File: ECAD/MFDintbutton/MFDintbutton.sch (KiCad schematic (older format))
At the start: 35 parts, among them J1 Conn_02x03_Odd_Even, J2 Conn_01x04, J3 Conn_01x04, J4 Conn_01x04, SW11 SW_Push, SW12 SW_Push, SW13 SW_Push, SW14 SW_Push, SW21 SW_Push, SW22 SW_Push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

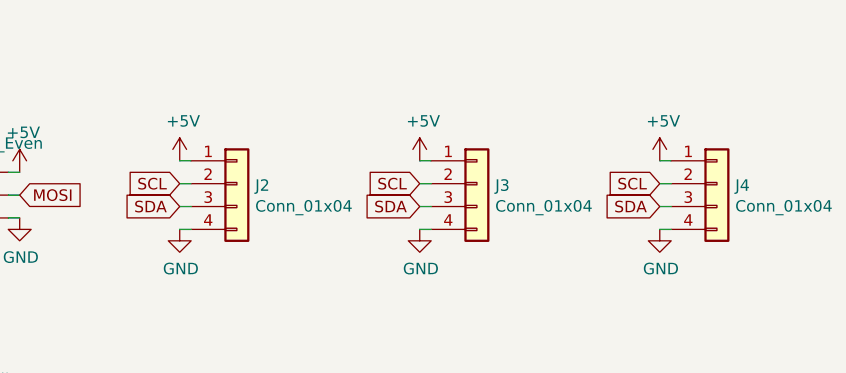
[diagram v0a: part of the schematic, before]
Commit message: Removing panelisations, adding polyfuses
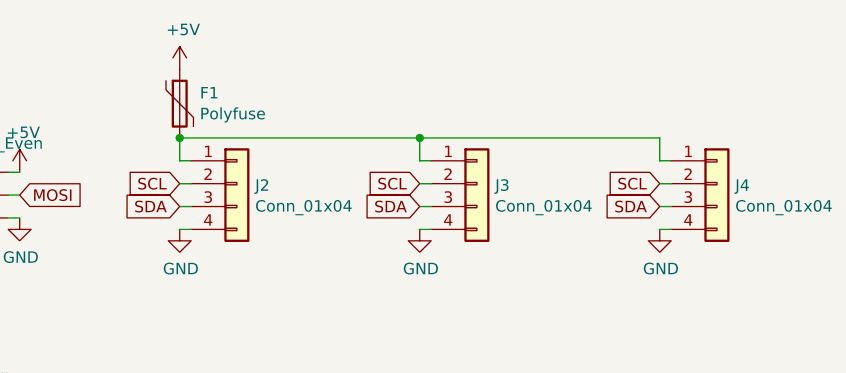
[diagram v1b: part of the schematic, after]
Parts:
- added F1: Polyfuse, Fuse:Fuse_1206_3216Metric_Pad1.42x1.75mm_HandSolder, symbol Device:Polyfuse
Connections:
- wire segments 141 -> 146
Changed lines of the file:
@@
 L power:+5V #PWR0104
 U 1 1 60C40200
-P 4650 1150
-F 0 "#PWR0104" H 4650 1000 50  0001 C CNN
-F 1 "+5V" H 4665 1323 50  0000 C CNN
-F 2 "" H 4650 1150 50  0001 C CNN
-F 3 "" H 4650 1150 50  0001 C CNN
-	1    4650 1150
+P 4650 750
+F 0 "#PWR0104" H 4650 600 50  0001 C CNN
+F 1 "+5V" H 4665 923 50  0000 C CNN
+F 2 "" H 4650 750 50  0001 C CNN
+F 3 "" H 4650 750 50  0001 C CNN
+	1    4650 750
 	1    0    0    -1
 $EndComp
@@
 	1    0    0    -1
 $EndComp
-$Comp
-L power:+5V #PWR0112
-U 1 1 60D32708
-P 5700 1150
-F 0 "#PWR0112" H 5700 1000 50  0001 C CNN
-F 1 "+5V" H 5715 1323 50  0000 C CNN
-F 2 "" H 5700 1150 50  0001 C CNN
-F 3 "" H 5700 1150 50  0001 C CNN
-	1    5700 1150
-	1    0    0    -1
-$EndComp
 Wire Wire Line
 	5700 1150 5750 1150
@@
 	1    0    0    -1
 $EndComp
-$Comp
-L power:+5V #PWR0114
-U 1 1 60D3B723
-P 6750 1150
-F 0 "#PWR0114" H 6750 1000 50  0001 C CNN
-F 1 "+5V" H 6765 1323 50  0000 C CNN
-F 2 "" H 6750 1150 50  0001 C CNN
-F 3 "" H 6750 1150 50  0001 C CNN
-	1    6750 1150
-	1    0    0    -1
-$EndComp
 Wire Wire Line
 	6750 1150 6800 1150
@@
 Wire Wire Line
 	6800 1450 6750 1450
+Wire Wire Line
+	6750 1150 6750 1050
+Wire Wire Line
+	6750 1050 5700 1050
+Wire Wire Line
+	5700 1050 5700 1150
+Wire Wire Line
+	4650 1150 4650 1050
+Wire Wire Line
+	4650 1050 5700 1050
+Connection ~ 5700 1050
+$Comp
+L Device:Polyfuse F1
+U 1 1 60FA5A26
+P 4650 900
+F 0 "F1" H 4738 946 50  0000 L CNN
+F 1 "Polyfuse" H 4738 855 50  0000 L CNN
+F 2 "Fuse:Fuse_1206_3216Metric_Pad1.42x1.75mm_HandSolder" H 4700 700 50  0001 L CNN
+F 3 "~" H 4650 900 50  0001 C CNN
+	1    4650 900
+	1    0    0    -1
+$EndComp
+Connection ~ 4650 1050
 $EndSCHEMATC

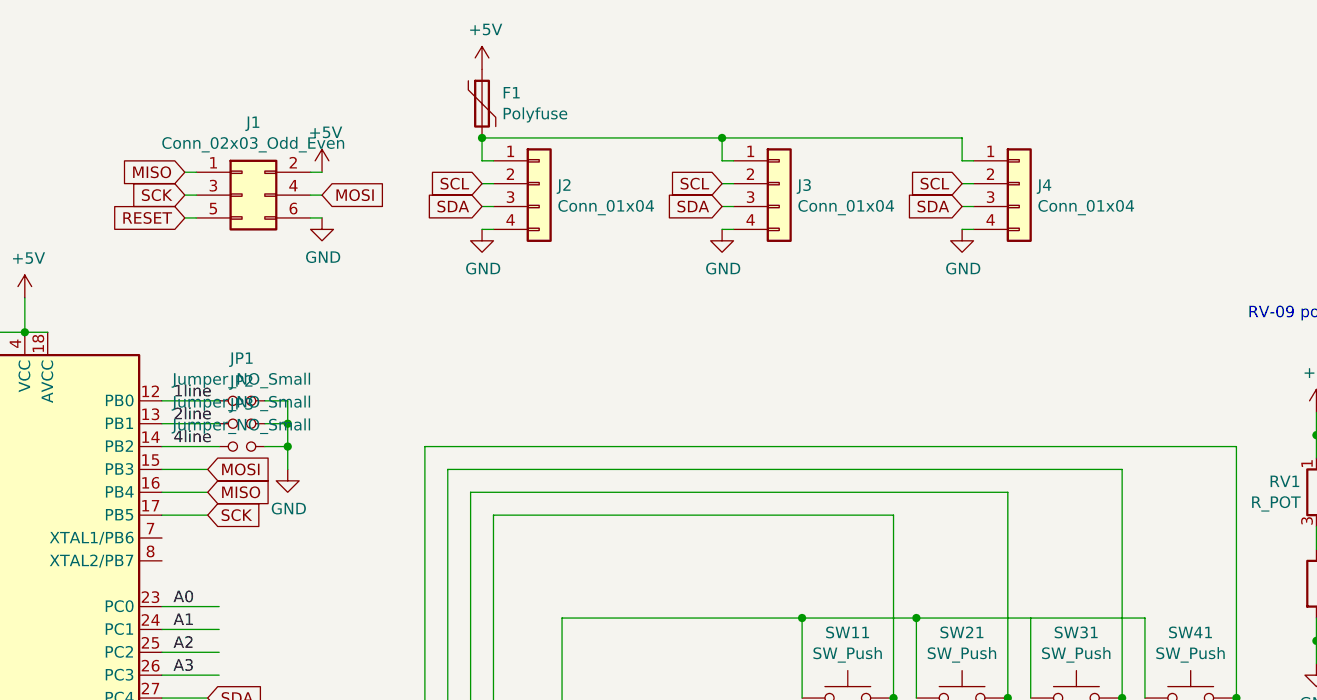
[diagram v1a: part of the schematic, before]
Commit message: Change from 1x04 2.54mm headers to 1x05 micro JST
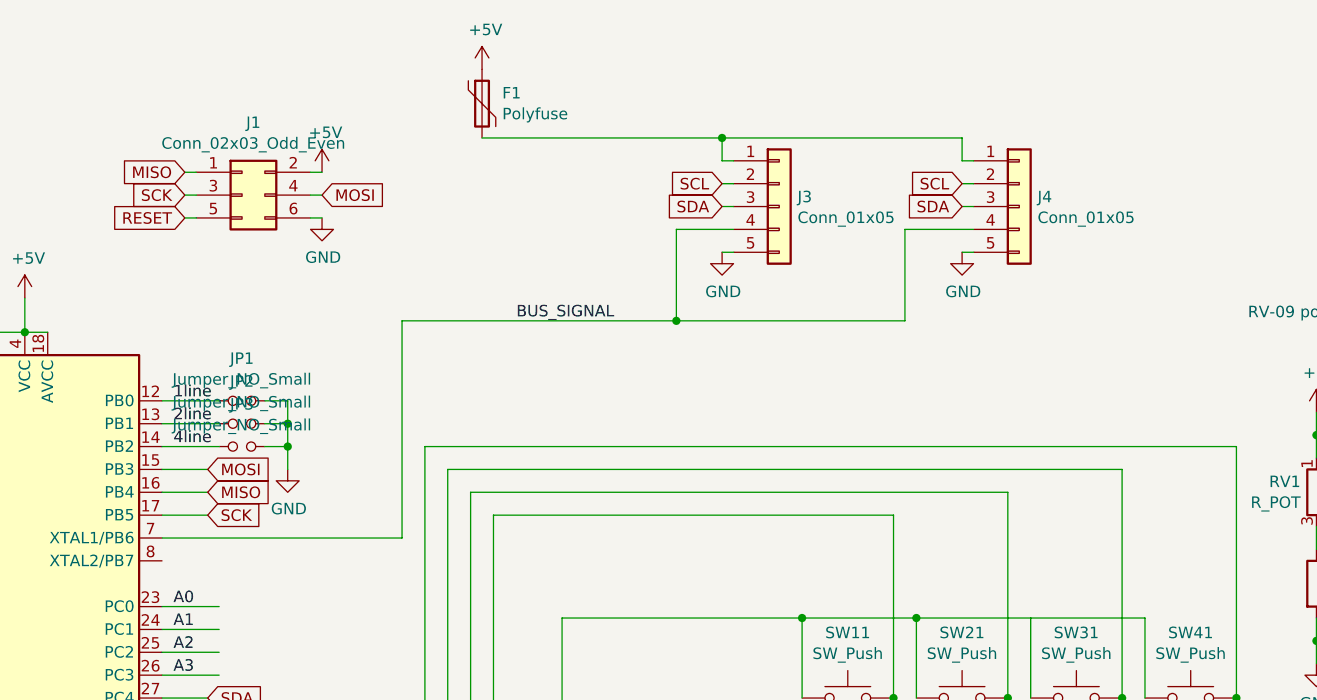
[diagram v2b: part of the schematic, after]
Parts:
- removed J2, J3, J4: Conn_01x04, mycustomlibrary:PinHeader_1x04_P2.54mm_Horizontal_SMD, symbol Connector_Generic:Conn_01x04
- added J3, J4: Conn_01x05, Connector_JST:JST_GH_SM05B-GHS-TB_1x05-1MP_P1.25mm_Horizontal, symbol Connector_Generic:Conn_01x05
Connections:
- net labels added: BUS_SIGNAL
- wire segments 146 -> 149
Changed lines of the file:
@@
 $EndDescr
-$Comp
-L Connector_Generic:Conn_01x04 J2
-U 1 1 60C3EB30
-P 4900 1250
-F 0 "J2" H 4980 1242 50  0000 L CNN
-F 1 "Conn_01x04" H 4980 1151 50  0000 L CNN
-F 2 "mycustomlibrary:PinHeader_1x04_P2.54mm_Horizontal_SMD" H 4900 1250 50  0001 C CNN
-F 3 "~" H 4900 1250 50  0001 C CNN
-	1    4900 1250
-	1    0    0    -1
-$EndComp
-Text GLabel 4650 1250 0    50   Input ~ 0
-SCL
-Text GLabel 4650 1350 0    50   Input ~ 0
-SDA
-$Comp
-L power:GND #PWR0103
-U 1 1 60C3FBB7
-P 4650 1450
-F 0 "#PWR0103" H 4650 1200 50  0001 C CNN
-F 1 "GND" H 4655 1277 50  0000 C CNN
-F 2 "" H 4650 1450 50  0001 C CNN
-F 3 "" H 4650 1450 50  0001 C CNN
-	1    4650 1450
-	1    0    0    -1
-$EndComp
 $Comp
 L power:+5V #PWR0104
@@
 	1    0    0    -1
 $EndComp
-Wire Wire Line
-	4650 1150 4700 1150
-Wire Wire Line
-	4700 1250 4650 1250
-Wire Wire Line
-	4650 1350 4700 1350
-Wire Wire Line
-	4700 1450 4650 1450
 $Comp
 L Connector_Generic:Conn_02x03_Odd_Even J1
@@
 	1    0    0    -1
 $EndComp
-$Comp
-L Connector_Generic:Conn_01x04 J3
-U 1 1 60D326FA
-P 5950 1250
-F 0 "J3" H 6030 1242 50  0000 L CNN
-F 1 "Conn_01x04" H 6030 1151 50  0000 L CNN
-F 2 "mycustomlibrary:PinHeader_1x04_P2.54mm_Horizontal_SMD" H 5950 1250 50  0001 C CNN
-F 3 "~" H 5950 1250 50  0001 C CNN
-	1    5950 1250
-	1    0    0    -1
-$EndComp
 Text GLabel 5700 1250 0    50   Input ~ 0
 SCL
@@
 L power:GND #PWR0111
 U 1 1 60D32702
-P 5700 1450
-F 0 "#PWR0111" H 5700 1200 50  0001 C CNN
-F 1 "GND" H 5705 1277 50  0000 C CNN
-F 2 "" H 5700 1450 50  0001 C CNN
-F 3 "" H 5700 1450 50  0001 C CNN
-	1    5700 1450
+P 5700 1550
+F 0 "#PWR0111" H 5700 1300 50  0001 C CNN
+F 1 "GND" H 5705 1377 50  0000 C CNN
+F 2 "" H 5700 1550 50  0001 C CNN
+F 3 "" H 5700 1550 50  0001 C CNN
+	1    5700 1550
 	1    0    0    -1
 $EndComp
@@
 	5700 1350 5750 1350
 Wire Wire Line
-	5750 1450 5700 1450
-$Comp
-L Connector_Generic:Conn_01x04 J4
-U 1 1 60D3B715
-P 7000 1250
-F 0 "J4" H 7080 1242 50  0000 L CNN
-F 1 "Conn_01x04" H 7080 1151 50  0000 L CNN
-F 2 "mycustomlibrary:PinHeader_1x04_P2.54mm_Horizontal_SMD" H 7000 1250 50  0001 C CNN
-F 3 "~" H 7000 1250 50  0001 C CNN
-	1    7000 1250
-	1    0    0    -1
-$EndComp
+	5750 1550 5700 1550
 Text GLabel 6750 1250 0    50   Input ~ 0
 SCL
@@
 L power:GND #PWR0113
 U 1 1 60D3B71D
-P 6750 1450
-F 0 "#PWR0113" H 6750 1200 50  0001 C CNN
-F 1 "GND" H 6755 1277 50  0000 C CNN
-F 2 "" H 6750 1450 50  0001 C CNN
-F 3 "" H 6750 1450 50  0001 C CNN
-	1    6750 1450
+P 6750 1550
+F 0 "#PWR0113" H 6750 1300 50  0001 C CNN
+F 1 "GND" H 6755 1377 50  0000 C CNN
+F 2 "" H 6750 1550 50  0001 C CNN
+F 3 "" H 6750 1550 50  0001 C CNN
+	1    6750 1550
 	1    0    0    -1
 $EndComp
@@
 	6750 1350 6800 1350
 Wire Wire Line
-	6800 1450 6750 1450
+	6800 1550 6750 1550
 Wire Wire Line
 	6750 1150 6750 1050
@@
 Wire Wire Line
 	5700 1050 5700 1150
-Wire Wire Line
-	4650 1150 4650 1050
 Wire Wire Line
 	4650 1050 5700 1050
@@
 	1    0    0    -1
 $EndComp
-Connection ~ 4650 1050
+$Comp
+L Connector_Generic:Conn_01x05 J3
+U 1 1 6115CCBA
+P 5950 1350
+F 0 "J3" H 6030 1392 50  0000 L CNN
+F 1 "Conn_01x05" H 6030 1301 50  0000 L CNN
+F 2 "Connector_JST:JST_GH_SM05B-GHS-TB_1x05-1MP_P1.25mm_Horizontal" H 5950 1350 50  0001 C CNN
+F 3 "~" H 5950 1350 50  0001 C CNN
+	1    5950 1350
+	1    0    0    -1
+$EndComp
+$Comp
+L Connector_Generic:Conn_01x05 J4
+U 1 1 611637B6
+P 7000 1350
+F 0 "J4" H 7080 1392 50  0000 L CNN
+F 1 "Conn_01x05" H 7080 1301 50  0000 L CNN
+F 2 "Connector_JST:JST_GH_SM05B-GHS-TB_1x05-1MP_P1.25mm_Horizontal" H 7000 1350 50  0001 C CNN
+F 3 "~" H 7000 1350 50  0001 C CNN
+	1    7000 1350
+	1    0    0    -1
+$EndComp
+Wire Wire Line
+	3250 2800 4300 2800
+Wire Wire Line
+	4300 2800 4300 1850
+Wire Wire Line
+	5750 1450 5500 1450
+Wire Wire Line
+	5500 1450 5500 1850
+Wire Wire Line
+	5500 1850 4300 1850
+Wire Wire Line
+	5500 1850 6500 1850
+Wire Wire Line
+	6500 1850 6500 1450
+Wire Wire Line
+	6500 1450 6800 1450
+Connection ~ 5500 1850
+Text Label 4800 1850 0    50   ~ 0
+BUS_SIGNAL
 $EndSCHEMATC

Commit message: Swap bus connector to 4-pin JST-GH
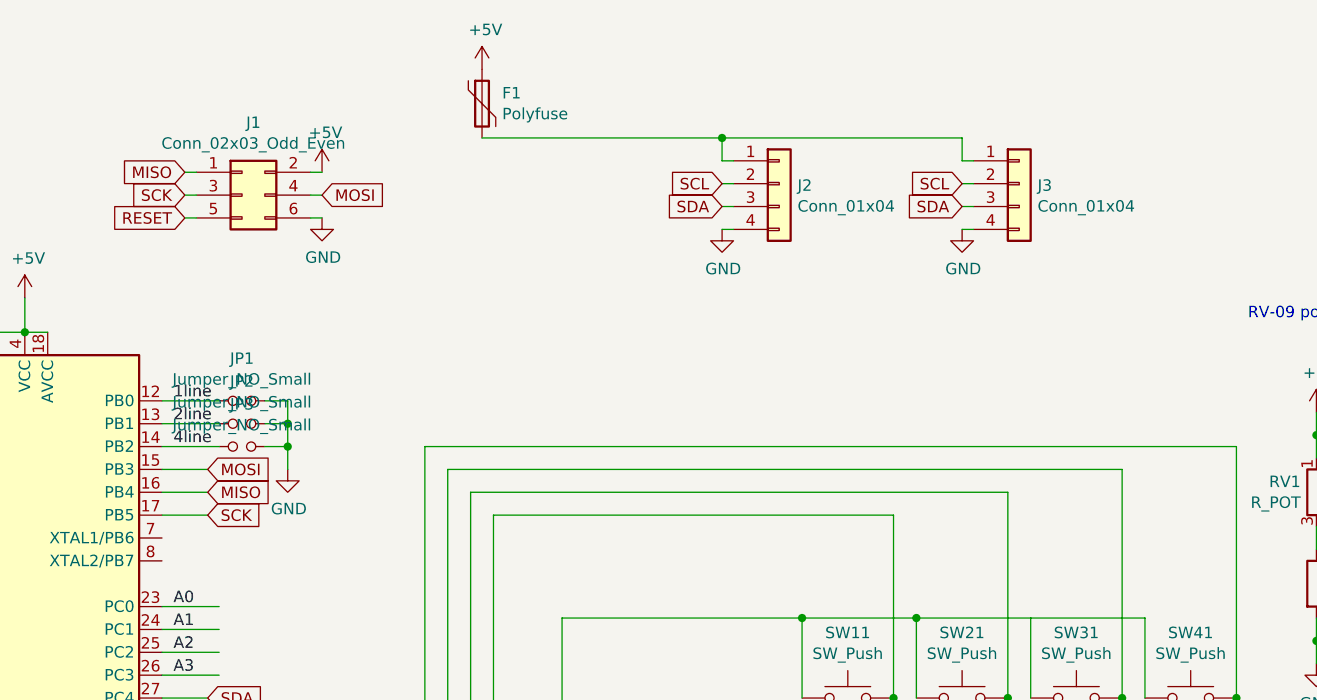
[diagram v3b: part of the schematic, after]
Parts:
- removed J3, J4: Conn_01x05, Connector_JST:JST_GH_SM05B-GHS-TB_1x05-1MP_P1.25mm_Horizontal, symbol Connector_Generic:Conn_01x05
- added J2, J3: Conn_01x04, Connector_JST:JST_GH_SM04B-GHS-TB_1x04-1MP_P1.25mm_Horizontal, symbol Connector_Generic:Conn_01x04
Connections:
- net labels removed: BUS_SIGNAL
- wire segments 149 -> 141
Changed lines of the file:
@@
 L power:GND #PWR0111
 U 1 1 60D32702
-P 5700 1550
-F 0 "#PWR0111" H 5700 1300 50  0001 C CNN
-F 1 "GND" H 5705 1377 50  0000 C CNN
-F 2 "" H 5700 1550 50  0001 C CNN
-F 3 "" H 5700 1550 50  0001 C CNN
-	1    5700 1550
+P 5700 1450
+F 0 "#PWR0111" H 5700 1200 50  0001 C CNN
+F 1 "GND" H 5705 1277 50  0000 C CNN
+F 2 "" H 5700 1450 50  0001 C CNN
+F 3 "" H 5700 1450 50  0001 C CNN
+	1    5700 1450
 	1    0    0    -1
 $EndComp
@@
 	5700 1350 5750 1350
 Wire Wire Line
-	5750 1550 5700 1550
+	5750 1450 5700 1450
 Text GLabel 6750 1250 0    50   Input ~ 0
 SCL
@@
 L power:GND #PWR0113
 U 1 1 60D3B71D
-P 6750 1550
-F 0 "#PWR0113" H 6750 1300 50  0001 C CNN
-F 1 "GND" H 6755 1377 50  0000 C CNN
-F 2 "" H 6750 1550 50  0001 C CNN
-F 3 "" H 6750 1550 50  0001 C CNN
-	1    6750 1550
+P 6750 1450
+F 0 "#PWR0113" H 6750 1200 50  0001 C CNN
+F 1 "GND" H 6755 1277 50  0000 C CNN
+F 2 "" H 6750 1450 50  0001 C CNN
+F 3 "" H 6750 1450 50  0001 C CNN
+	1    6750 1450
 	1    0    0    -1
 $EndComp
@@
 	6750 1350 6800 1350
 Wire Wire Line
-	6800 1550 6750 1550
+	6800 1450 6750 1450
 Wire Wire Line
 	6750 1150 6750 1050
@@
 $EndComp
 $Comp
-L Connector_Generic:Conn_01x05 J3
-U 1 1 6115CCBA
-P 5950 1350
-F 0 "J3" H 6030 1392 50  0000 L CNN
-F 1 "Conn_01x05" H 6030 1301 50  0000 L CNN
-F 2 "Connector_JST:JST_GH_SM05B-GHS-TB_1x05-1MP_P1.25mm_Horizontal" H 5950 1350 50  0001 C CNN
-F 3 "~" H 5950 1350 50  0001 C CNN
-	1    5950 1350
+L Connector_Generic:Conn_01x04 J2
+U 1 1 61254333
+P 5950 1250
+F 0 "J2" H 6030 1242 50  0000 L CNN
+F 1 "Conn_01x04" H 6030 1151 50  0000 L CNN
+F 2 "Connector_JST:JST_GH_SM04B-GHS-TB_1x04-1MP_P1.25mm_Horizontal" H 5950 1250 50  0001 C CNN
+F 3 "~" H 5950 1250 50  0001 C CNN
+	1    5950 1250
 	1    0    0    -1
 $EndComp
 $Comp
-L Connector_Generic:Conn_01x05 J4
-U 1 1 611637B6
-P 7000 1350
-F 0 "J4" H 7080 1392 50  0000 L CNN
-F 1 "Conn_01x05" H 7080 1301 50  0000 L CNN
-F 2 "Connector_JST:JST_GH_SM05B-GHS-TB_1x05-1MP_P1.25mm_Horizontal" H 7000 1350 50  0001 C CNN
-F 3 "~" H 7000 1350 50  0001 C CNN
-	1    7000 1350
+L Connector_Generic:Conn_01x04 J3
+U 1 1 61255AE8
+P 7000 1250
+F 0 "J3" H 7080 1242 50  0000 L CNN
+F 1 "Conn_01x04" H 7080 1151 50  0000 L CNN
+F 2 "Connector_JST:JST_GH_SM04B-GHS-TB_1x04-1MP_P1.25mm_Horizontal" H 7000 1250 50  0001 C CNN
+F 3 "~" H 7000 1250 50  0001 C CNN
+	1    7000 1250
 	1    0    0    -1
 $EndComp
-Wire Wire Line
-	3250 2800 4300 2800
-Wire Wire Line
-	4300 2800 4300 1850
-Wire Wire Line
-	5750 1450 5500 1450
-Wire Wire Line
-	5500 1450 5500 1850
-Wire Wire Line
-	5500 1850 4300 1850
-Wire Wire Line
-	5500 1850 6500 1850
-Wire Wire Line
-	6500 1850 6500 1450
-Wire Wire Line
-	6500 1450 6800 1450
-Connection ~ 5500 1850
-Text Label 4800 1850 0    50   ~ 0
-BUS_SIGNAL
 $EndSCHEMATC
